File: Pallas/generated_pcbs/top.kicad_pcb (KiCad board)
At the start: 2 copper layers, 467.5 x 140 mm, 19 parts

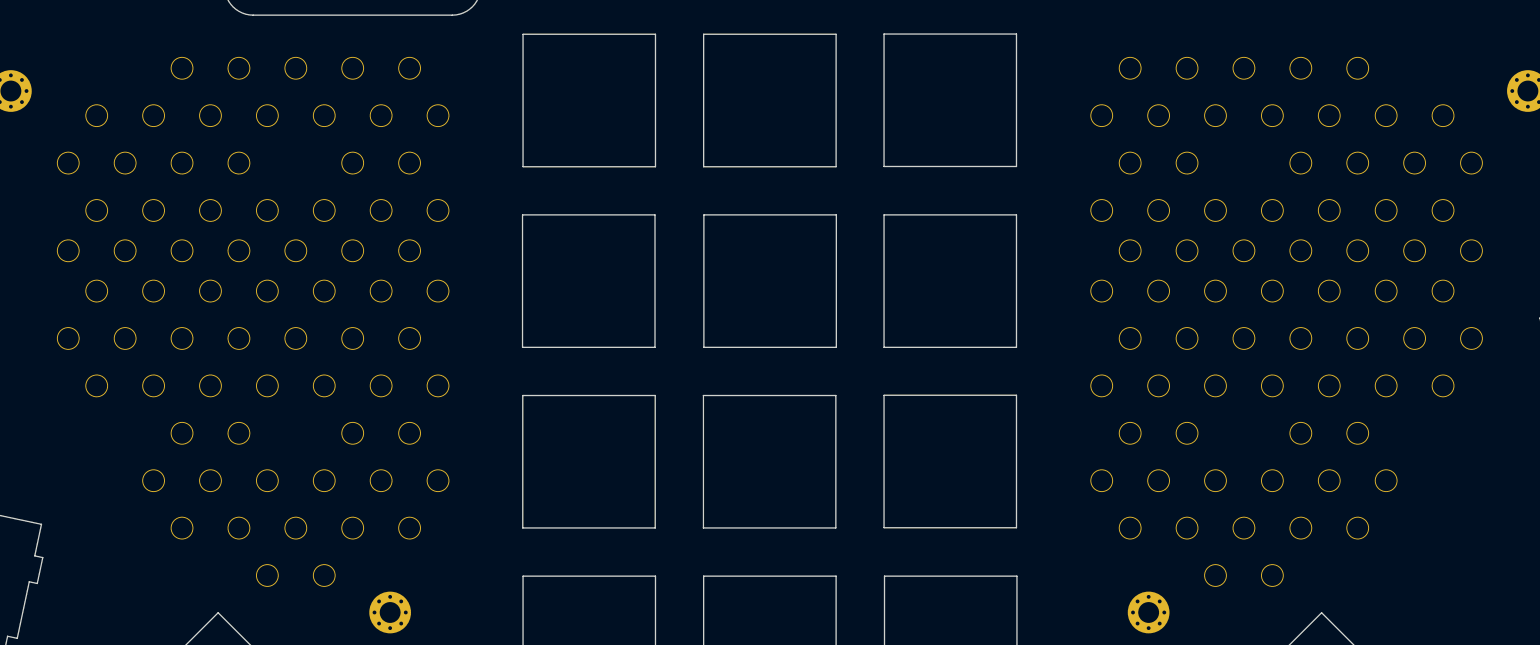
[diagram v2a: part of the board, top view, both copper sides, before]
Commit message: update RGB led footprint and route
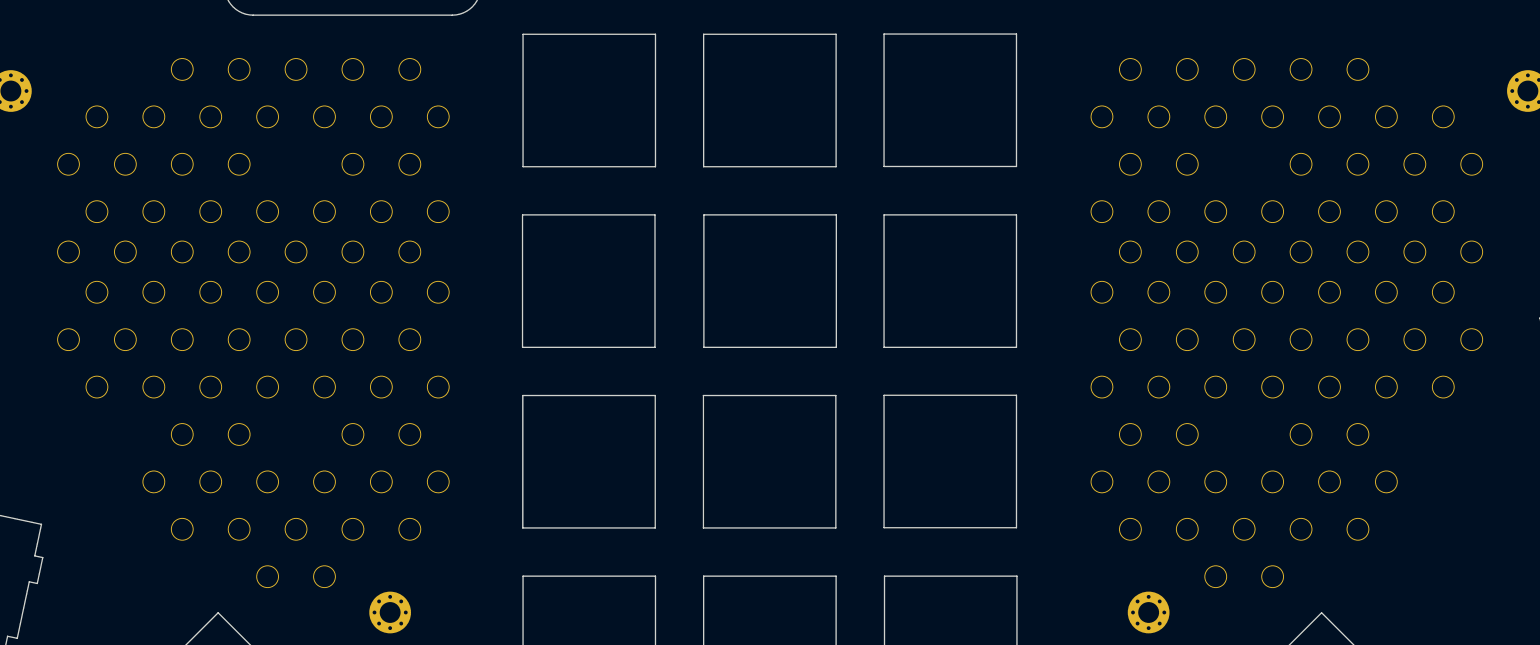
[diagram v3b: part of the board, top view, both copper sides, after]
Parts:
- moved DecorationHoleTop1 0.13 mm to (238.9, 114.1)
- moved DecorationHoleTop2 0.13 mm to (338.9, 114.1)

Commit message: Pallas rev 0.3
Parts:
- moved DecorationHoleTop1 0.18 mm to (238.9, 114.3)
- moved DecorationHoleTop2 0.18 mm to (338.9, 114.3)
